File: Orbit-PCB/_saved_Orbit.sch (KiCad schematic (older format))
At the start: 294 parts, among them J1 PJ-3200B-4A, J10 Breakaway_Tabs, J11 PJ-3200B-4A, J12 AVR-ISP-6, J13 Breakaway_Tabs, J14 Breakaway_Tabs, J17 Breakaway_Tabs, J18 Breakaway_Tabs, J19 Breakaway_Tabs, J2 AVR-ISP-6, J20 Breakaway_Tabs, J3 Breakaway_Tabs, J5 Breakaway_Tabs, J6 Breakaway_Tabs, J7 Breakaway_Tabs, J9 Breakaway_Tabs, Q1 2N7002, Q2 2N7002, SW1 SW_Push, SW2 SW_Push, U1 ATmega32U4-MU, U2 PRTR5V0U2X, U3 ATmega32U4-MU, U4 PRTR5V0U2X, Y1 16MHz, Y2 16MHz

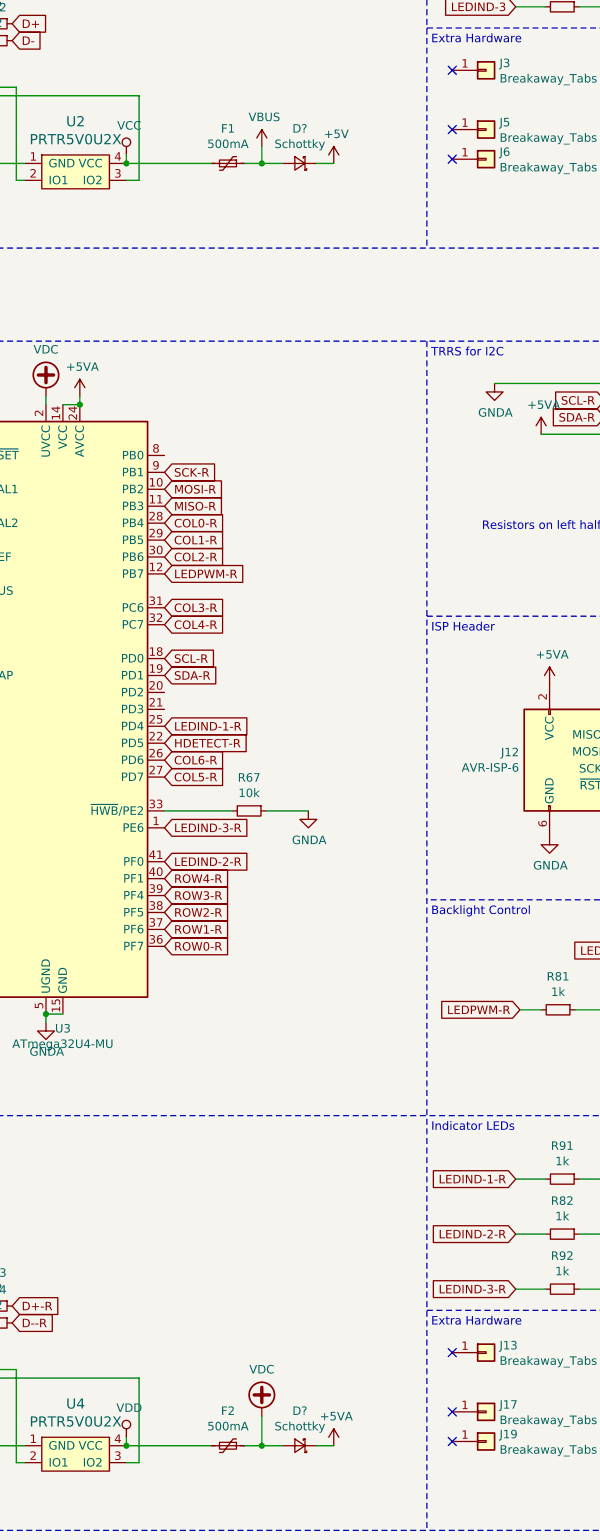
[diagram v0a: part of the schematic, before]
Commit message: Add schottky divide to vcc/vbus
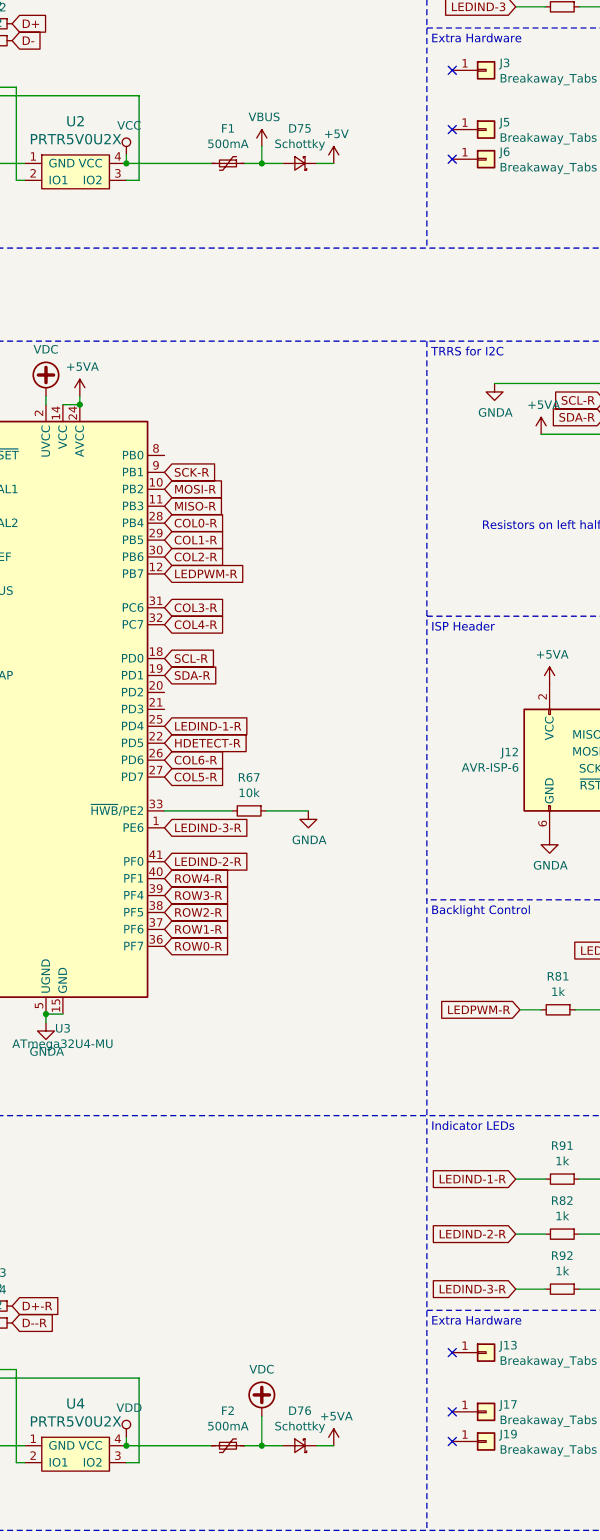
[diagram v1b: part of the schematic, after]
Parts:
- gave numbers to parts that had none: 2
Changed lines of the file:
@@
 	2325 8925 2900 8925
 $Comp
-L Device:D_Schottky_Small D?
+L Device:D_Schottky_Small D75
 U 1 1 5BF8426A
 P 4900 7200
-F 0 "D?" H 4900 6995 50  0000 C CNN
+F 0 "D75" H 4900 6995 50  0000 C CNN
 F 1 "Schottky" H 4900 7086 50  0000 C CNN
 F 2 "Diodes_SMD:D_SOD-123" V 4900 7200 50  0001 C CNN
@@
 	5100 7200 5000 7200
 $Comp
-L power:VBUS #PWR?
+L power:VBUS #PWR0104
 U 1 1 5C001278
 P 4675 7100
-F 0 "#PWR?" H 4675 6950 50  0001 C CNN
+F 0 "#PWR0104" H 4675 6950 50  0001 C CNN
 F 1 "VBUS" H 4690 7273 50  0000 C CNN
 F 2 "" H 4675 7100 50  0001 C CNN
@@
 	4675 7200 4575 7200
 $Comp
-L Device:D_Schottky_Small D?
+L Device:D_Schottky_Small D76
 U 1 1 5C07FDD0
 P 4900 14775
-F 0 "D?" H 4900 14570 50  0000 C CNN
+F 0 "D76" H 4900 14570 50  0000 C CNN
 F 1 "Schottky" H 4900 14661 50  0000 C CNN
 F 2 "Diodes_SMD:D_SOD-123" V 4900 14775 50  0001 C CNN
@@
 	5100 14775 5000 14775
 $Comp
-L power:VDC #PWR?
+L power:VDC #PWR0107
 U 1 1 5C1030A0
 P 4675 14600
-F 0 "#PWR?" H 4675 14500 50  0001 C CNN
+F 0 "#PWR0107" H 4675 14500 50  0001 C CNN
 F 1 "VDC" H 4675 14875 50  0000 C CNN
 F 2 "" H 4675 14600 50  0001 C CNN
@@
 Connection ~ 3600 8625
 $Comp
-L power:VDC #PWR?
+L power:VDC #PWR0138
 U 1 1 5C2FA9D3
 P 3400 8575
-F 0 "#PWR?" H 3400 8475 50  0001 C CNN
+F 0 "#PWR0138" H 3400 8475 50  0001 C CNN
 F 1 "VDC" H 3400 8850 50  0000 C CNN
 F 2 "" H 3400 8575 50  0001 C CNN
@@
 	3400 8575 3400 8625
 $Comp
-L power:VDC #PWR?
+L power:VDC #PWR0143
 U 1 1 5C378C46
 P 2625 9725
-F 0 "#PWR?" H 2625 9625 50  0001 C CNN
+F 0 "#PWR0143" H 2625 9625 50  0001 C CNN
 F 1 "VDC" H 2625 10000 50  0000 C CNN
 F 2 "" H 2625 9725 50  0001 C CNN
@@
 Connection ~ 3600 1050
 $Comp
-L power:VCC #PWR?
+L power:VCC #PWR0147
 U 1 1 5C476C25
 P 3400 1000
-F 0 "#PWR?" H 3400 850 50  0001 C CNN
+F 0 "#PWR0147" H 3400 850 50  0001 C CNN
 F 1 "VCC" H 3417 1173 50  0000 C CNN
 F 2 "" H 3400 1000 50  0001 C CNN
@@
 	3400 1000 3400 1050
 $Comp
-L power:VCC #PWR?
+L power:VCC #PWR0148
 U 1 1 5C4F4A47
 P 2625 2150
-F 0 "#PWR?" H 2625 2000 50  0001 C CNN
+F 0 "#PWR0148" H 2625 2000 50  0001 C CNN
 F 1 "VCC" H 2642 2323 50  0000 C CNN
 F 2 "" H 2625 2150 50  0001 C CNN

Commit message: Finish routing
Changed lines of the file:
@@
 	3600 1000 3600 1050
 Connection ~ 3600 1050
+Wire Wire Line
+	3400 1000 3400 1050
+Wire Wire Line
+	2625 2150 2900 2150
 $Comp
-L power:VCC #PWR0147
-U 1 1 5C476C25
+L power:VBUS #PWR0147
+U 1 1 5BF23610
 P 3400 1000
 F 0 "#PWR0147" H 3400 850 50  0001 C CNN
-F 1 "VCC" H 3417 1173 50  0000 C CNN
+F 1 "VBUS" H 3415 1173 50  0000 C CNN
 F 2 "" H 3400 1000 50  0001 C CNN
 F 3 "" H 3400 1000 50  0001 C CNN
@@
 	1    0    0    -1
 $EndComp
-Wire Wire Line
-	3400 1000 3400 1050
 $Comp
-L power:VCC #PWR0148
-U 1 1 5C4F4A47
+L power:VBUS #PWR0148
+U 1 1 5BF2387E
 P 2625 2150
 F 0 "#PWR0148" H 2625 2000 50  0001 C CNN
-F 1 "VCC" H 2642 2323 50  0000 C CNN
+F 1 "VBUS" H 2640 2323 50  0000 C CNN
 F 2 "" H 2625 2150 50  0001 C CNN
 F 3 "" H 2625 2150 50  0001 C CNN
@@
 	1    0    0    -1
 $EndComp
-Wire Wire Line
-	2625 2150 2900 2150
 $EndSCHEMATC
